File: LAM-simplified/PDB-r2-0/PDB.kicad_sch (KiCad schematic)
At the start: 23 parts, among them J1 2.54mm 2x3, J10 xt60-female, J11 xt60-female, J12 xt60-female, J13 xt90-female, J14 xt90-female, J15 2.54mm 2x3, J2 2.54mm 2x3, J3 2.54mm 2x3, J5 xt30-female, J6 xt30-female, J7 xt60-female, J8 xt60-female, J9 xt60-female

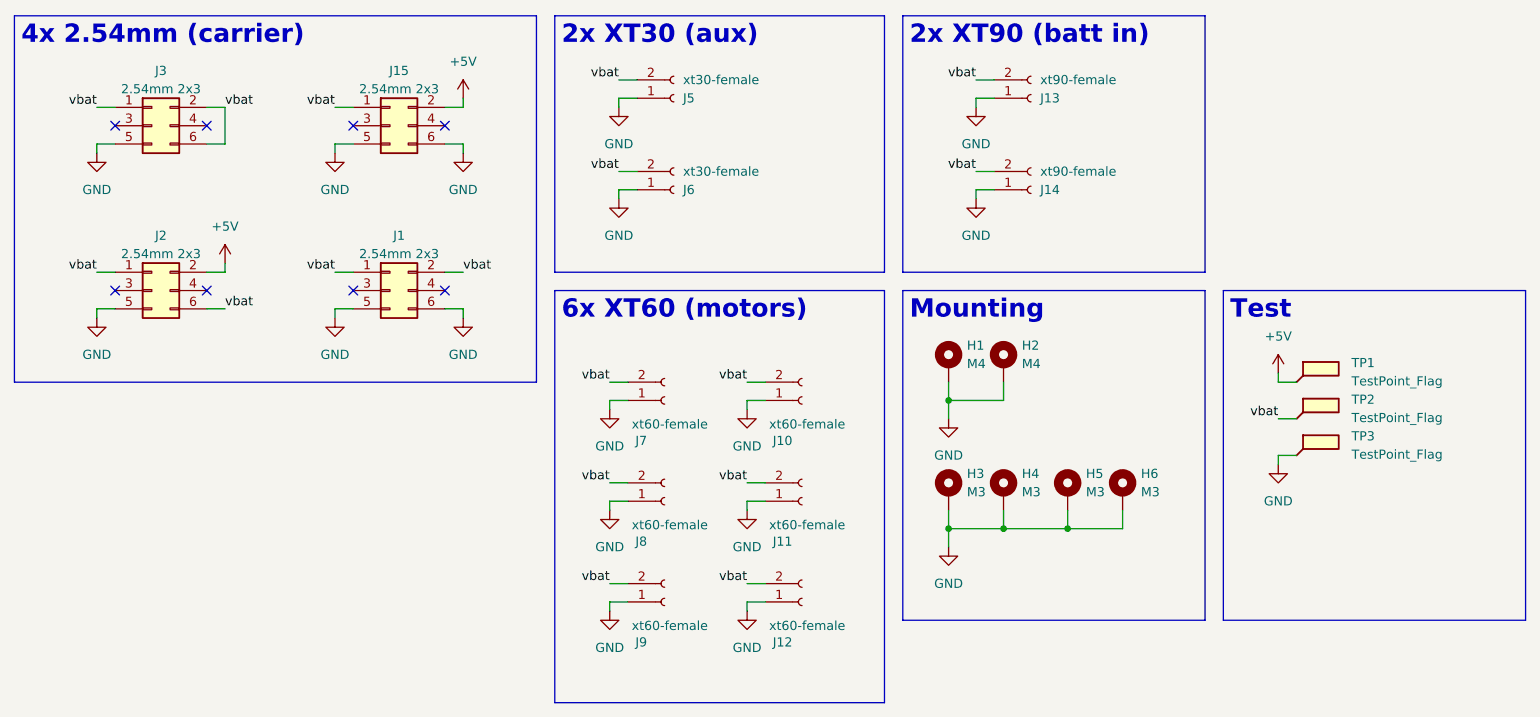
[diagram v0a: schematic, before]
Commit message: add AS150s to PDB r2.0
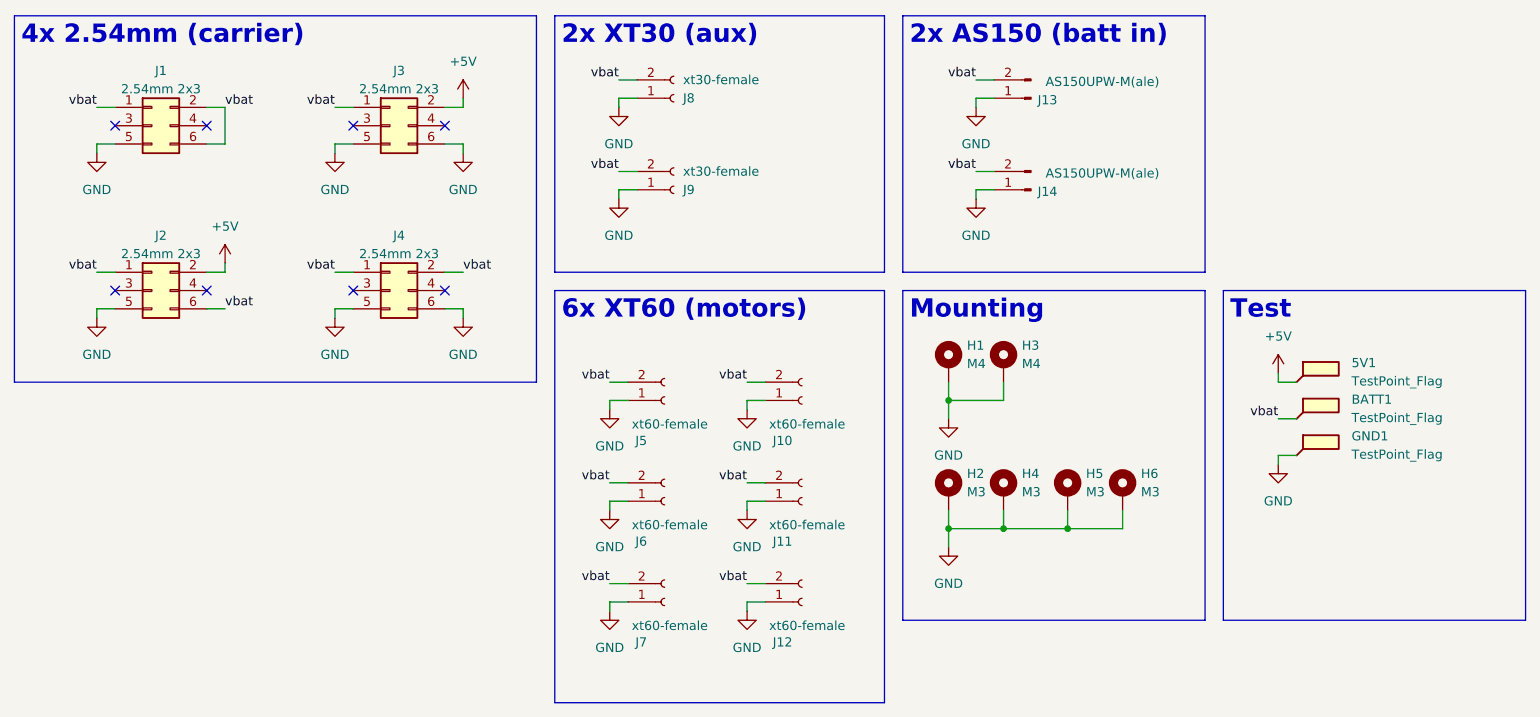
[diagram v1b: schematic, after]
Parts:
- removed J13, J14: xt90-female, Connector_AMASS:AMASS_XT90PW-M_1x02_P10.90mm_Horizontal, symbol Connector:Conn_01x02_Socket
- added J13, J14: AS150UPW-M(ale), aerpaw-footprints:AS150UPW(2+4-)M.G.Y, symbol Connector:Conn_01x02_Pin
- renumbered TP1 to 5V1, TP2 to BATT1, TP3 to GND1, H3 to H2, H2 to H3, J3 to J1, J15 to J3, J1 to J4, J7 to J5, J8 to J6, J9 to J7, J5 to J8, J6 to J9
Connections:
- net GND: now also J13.1 (Pin_1), J14.1 (Pin_1)
- net vbat: now also J13.2 (Pin_2), J14.2 (Pin_2)
